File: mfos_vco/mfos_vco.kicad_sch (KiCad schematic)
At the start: 26 parts, among them Q1 SSM2210, U1 OP275

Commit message: Second Commit
nueva hoja
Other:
- added sheet P2 (untitled.kicad_sch)
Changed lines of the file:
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@@
+		)
+	)
+	(sheet
+		(at 5.08 276.86)
+		(size 289.56 184.15)
+		(fields_autoplaced yes)
+		(stroke
+			(width 0.1524)
+			(type solid)
+		)
+		(fill
+			(color 0 0 0 0.0000)
+		)
+		(property "Sheetname" "P2"
+			(at 5.08 276.1484 0)
+			(effects
+				(font
+					(size 1.27 1.27)
+				)
+				(justify left bottom)
+			)
+		)
+		(property "Sheetfile" "untitled.kicad_sch"
+			(at 5.08 461.5946 0)
+			(effects
+				(font
+					(size 1.27 1.27)
+				)
+				(justify left top)
+			)
+		)
+		(instances
+			(project "mfos_vco"
+				(path "/db27d43e-bcf4-48a8-8785-18123cee165a"
+					(page "2")
+				)
+			)
 		)
 	)

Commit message: update
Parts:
- added C1: 100p, symbol Device:C_Polarized_US
- added R1: 10K, symbol Device:R_US
- added U2: TL072, symbol Amplifier_Operational:TL072
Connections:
- net +12V: now also U2.8 (V+)
- net -12V: now also U2.4 (V-)
- net GND: now also U2.3 (+)
- net at Q1.1 (C1): now also C1.1, U2.2 (-)
- new net: R1.1, U2.5 (+)
- new net: C1.2, R1.2, U2.1

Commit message: added gitignore and updated to kicad 9
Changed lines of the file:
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@@
 (kicad_sch
-	(version 20231120)
+	(version 20250114)
 	(generator "eeschema")
-	(generator_version "8.0")
+	(generator_version "9.0")
 	(paper "A4")
+	(text "COARSE\n"
+		(exclude_from_sim no)
+		(at 64.516 63.246 0)
+		(effects
+			(font
+				(size 1.27 1.27)
+			)
+		)
+	)
+	(text "FINE\n"
+		(exclude_from_sim no)
+		(at 74.676 50.546 0)
+		(effects
+			(font
+				(size 1.27 1.27)
+			)
+		)
+	)
 	(junction
 		(at 86.36 123.19)
@@
 		)
 	)
-	(text "COARSE\n"
-		(exclude_from_sim no)
-		(at 64.516 63.246 0)
-		(effects
-			(font
-				(size 1.27 1.27)
-			)
-		)
-	)
-	(text "FINE\n"
-		(exclude_from_sim no)
-		(at 74.676 50.546 0)
-		(effects
-			(font
-				(size 1.27 1.27)
-			)
-		)
-	)
 	(global_label "CV3"
 		(shape input)
@@
 		(at 5.08 276.86)
 		(size 289.56 184.15)
+		(exclude_from_sim no)
+		(in_bom yes)
+		(on_board yes)
+		(dnp no)
 		(fields_autoplaced yes)
 		(stroke
@@
 		)
 	)
+	(embedded_fonts no)
 )

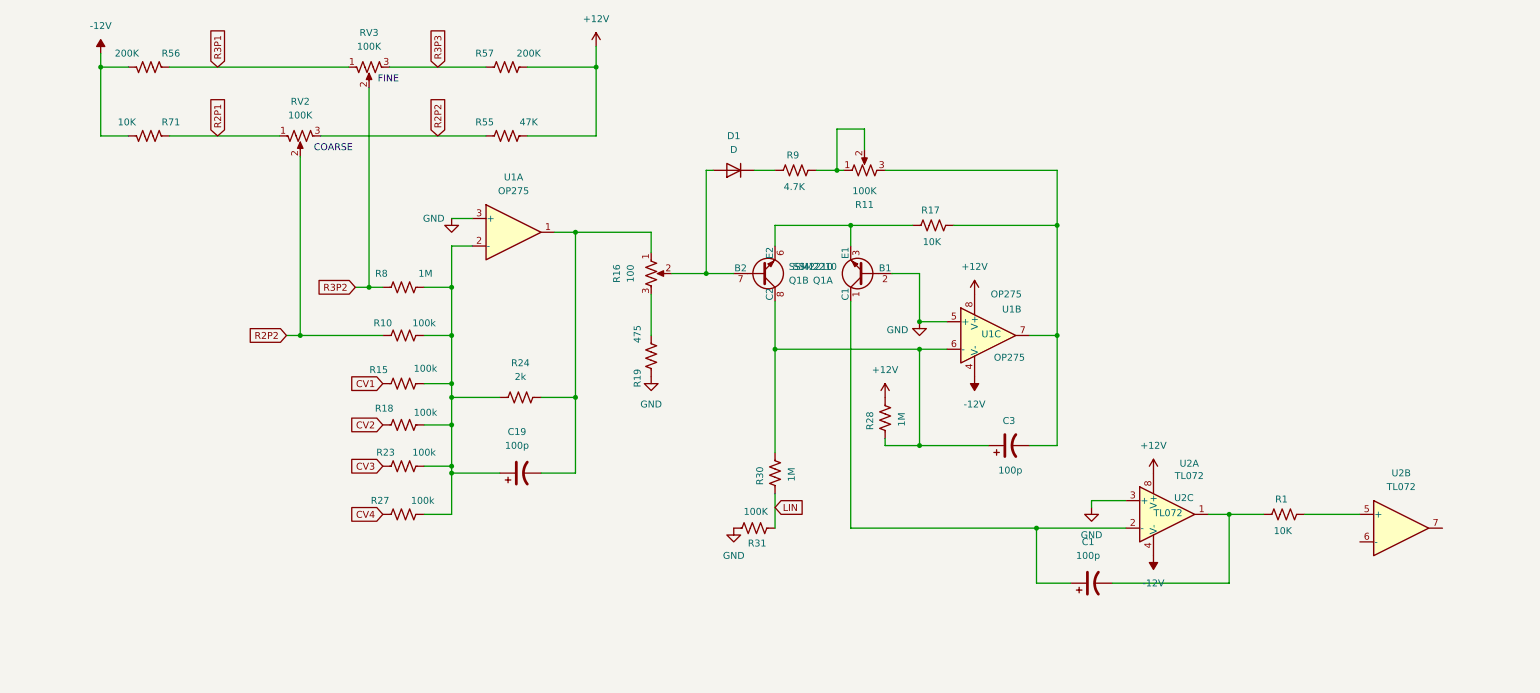
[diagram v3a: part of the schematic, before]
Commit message: finished first page. Added hierarchical sheets for first and second page
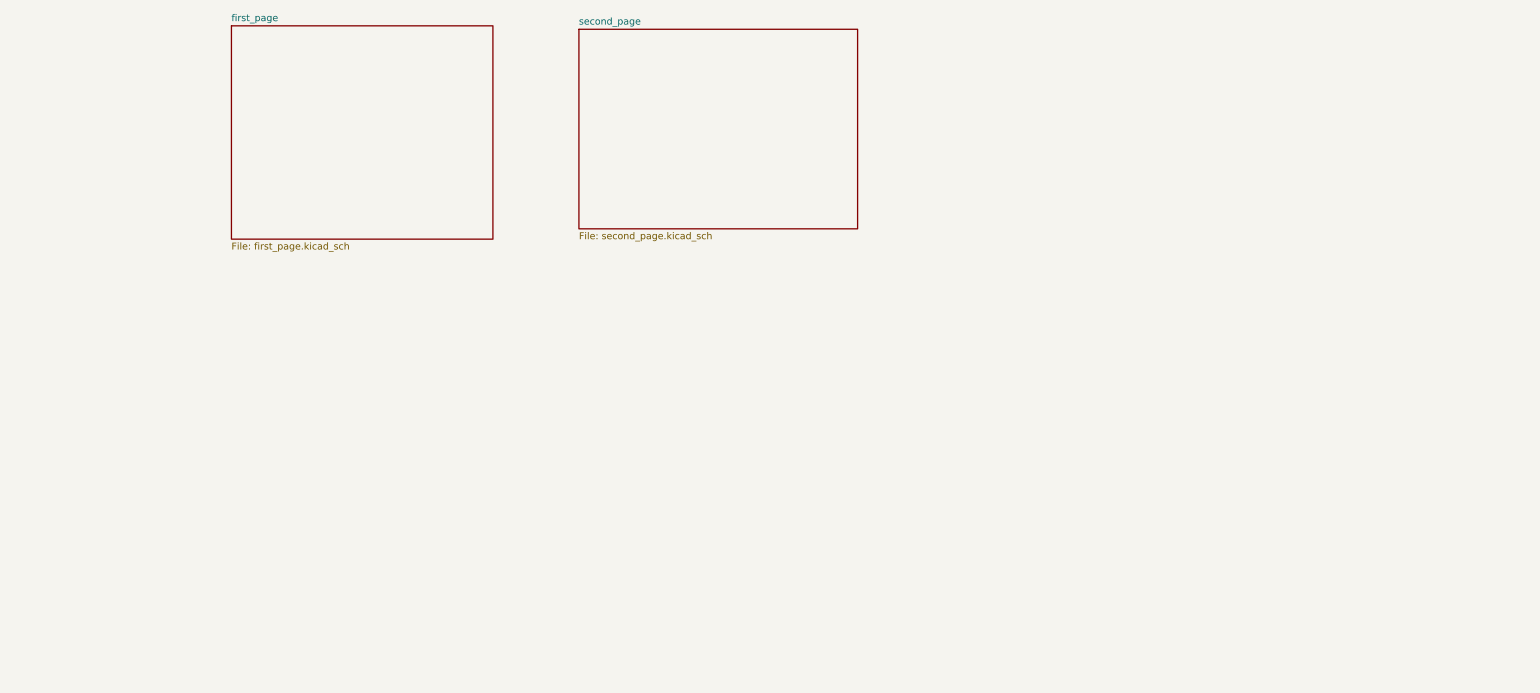
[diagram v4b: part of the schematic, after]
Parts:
- removed C1, C19, C3: 100p, symbol Device:C_Polarized_US
- removed D1: D, symbol Device:D
- removed Q1: SSM2210, symbol Transistor_BJT:SSM2210
- removed R1, R17, R71: 10K, symbol Device:R_US
- removed R10, R15, R18, R23, R27: 100k, symbol Device:R_US
- removed R11, RV2, RV3: 100K, symbol Device:R_Potentiometer_US
- removed R16: 100, symbol Device:R_Potentiometer_US
- removed R19: 475, symbol Device:R_US
- removed R24: 2k, symbol Device:R_US
- removed R28, R30, R8: 1M, symbol Device:R_US
- removed R31: 100K, symbol Device:R_US
- removed R55: 47K, symbol Device:R_US
- removed R56, R57: 200K, symbol Device:R_US
- removed R9: 4.7K, symbol Device:R_US
- removed U1: OP275, symbol Amplifier_Operational:OP275
- removed U2: TL072, symbol Amplifier_Operational:TL072
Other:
- added sheet first_page (first_page.kicad_sch)
- added sheet second_page (second_page.kicad_sch)
- note removed: "COARSE"
- note removed: "FINE"

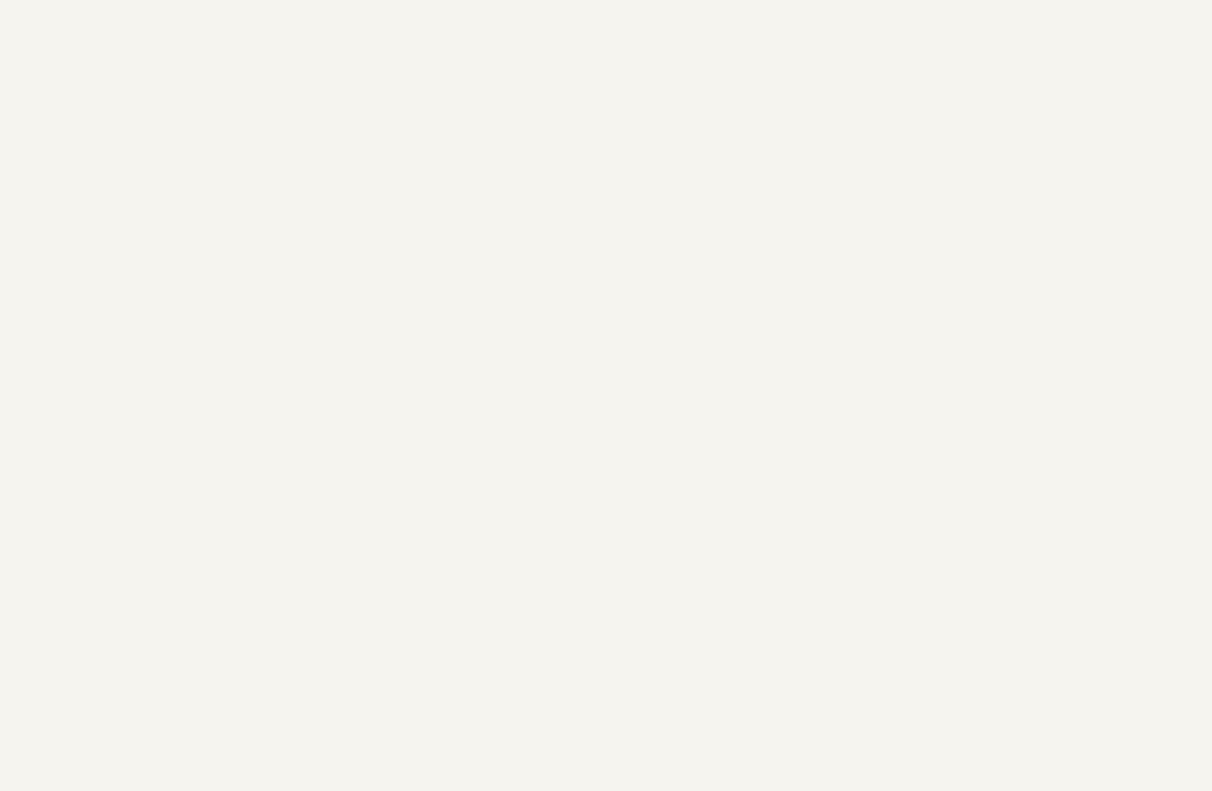
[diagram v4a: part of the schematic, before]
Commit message: Added output jumpers and custom foorprint
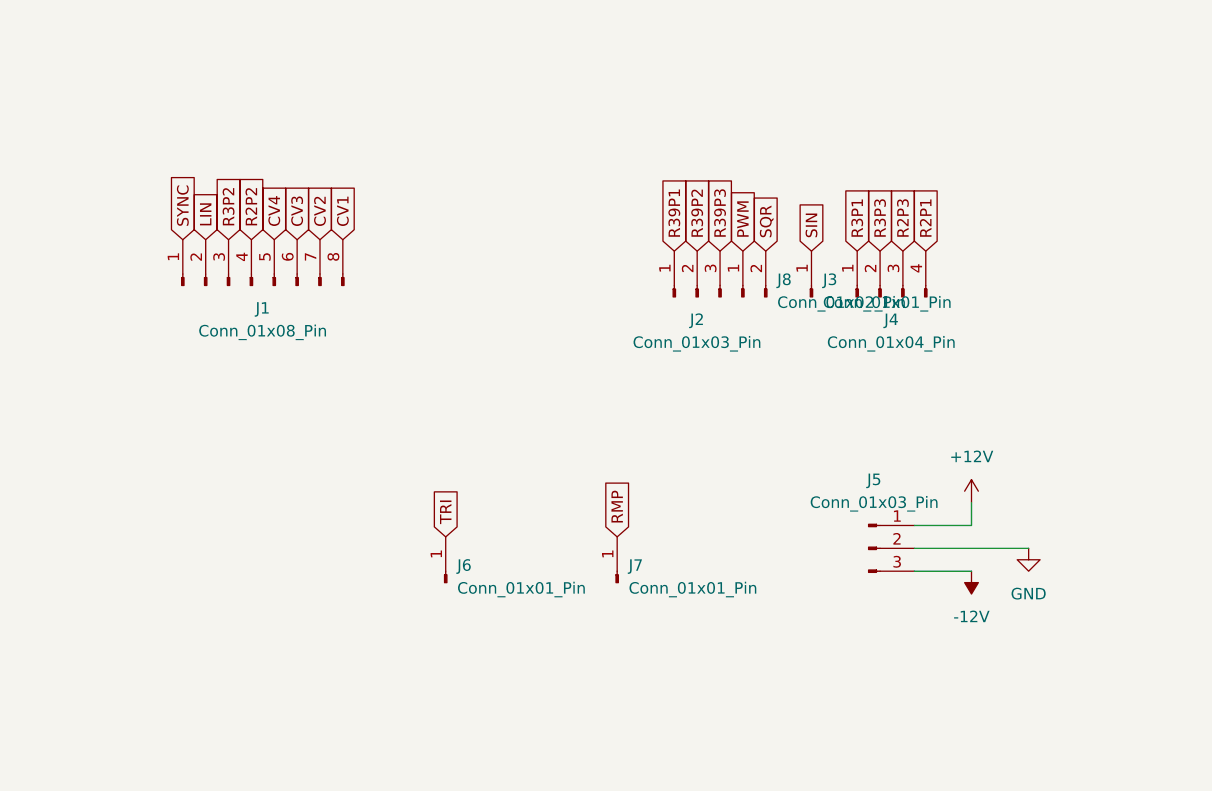
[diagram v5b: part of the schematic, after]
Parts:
- added J1: Conn_01x08_Pin, symbol Connector:Conn_01x08_Pin
- added J2, J5: Conn_01x03_Pin, symbol Connector:Conn_01x03_Pin
- added J3, J6, J7: Conn_01x01_Pin, symbol Connector:Conn_01x01_Pin
- added J4: Conn_01x04_Pin, symbol Connector:Conn_01x04_Pin
- added J8: Conn_01x02_Pin, symbol Connector:Conn_01x02_Pin
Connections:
- new net +12V: J5.1 (Pin_1)
- new net -12V: J5.3 (Pin_3)
- new net CV1: J1.8 (Pin_8)
- new net CV2: J1.7 (Pin_7)
- new net CV3: J1.6 (Pin_6)
- new net CV4: J1.5 (Pin_5)
- new net GND: J5.2 (Pin_2)
- new net LIN: J1.2 (Pin_2)
- new net PWM: J8.1 (Pin_1)
- new net R2P1: J4.4 (Pin_4)
- new net R2P2: J1.4 (Pin_4)
- new net R2P3: J4.3 (Pin_3)
- new net R39P1: J2.1 (Pin_1)
- new net R39P2: J2.2 (Pin_2)
- new net R39P3: J2.3 (Pin_3)
- new net R3P1: J4.1 (Pin_1)
- new net R3P2: J1.3 (Pin_3)
- new net R3P3: J4.2 (Pin_2)
- new net RMP: J7.1 (Pin_1)
- new net SIN: J3.1 (Pin_1)
- new net SQR: J8.2 (Pin_2)
- new net SYNC: J1.1 (Pin_1)
- new net TRI: J6.1 (Pin_1)

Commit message: added footprints
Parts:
- J1: footprint (none) -> Connector_PinSocket_2.54mm:PinSocket_1x08_P2.54mm_Vertical
- J2, J5: footprint (none) -> Connector_PinSocket_2.54mm:PinSocket_1x03_P2.54mm_Vertical
- J3, J6, J7: footprint (none) -> Connector_PinSocket_2.54mm:PinSocket_1x01_P2.54mm_Vertical
- J4: footprint (none) -> Connector_PinSocket_2.54mm:PinSocket_1x04_P2.54mm_Vertical
- J8: footprint (none) -> Connector_PinSocket_2.54mm:PinSocket_1x02_P2.54mm_Vertical
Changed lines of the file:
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@@
 			)
 		)
-		(property "Footprint" ""
+		(property "Footprint" "Connector_PinSocket_2.54mm:PinSocket_1x08_P2.54mm_Vertical"
 			(at 59.69 120.65 0)
 			(effects
@@
 			)
 		)
-		(property "Footprint" ""
+		(property "Footprint" "Connector_PinSocket_2.54mm:PinSocket_1x04_P2.54mm_Vertical"
 			(at 129.54 121.92 0)
 			(effects
@@
 			)
 		)
-		(property "Footprint" ""
+		(property "Footprint" "Connector_PinSocket_2.54mm:PinSocket_1x03_P2.54mm_Vertical"
 			(at 128.27 149.86 0)
 			(effects
@@
 			)
 		)
-		(property "Footprint" ""
+		(property "Footprint" "Connector_PinSocket_2.54mm:PinSocket_1x03_P2.54mm_Vertical"
 			(at 109.22 121.92 0)
 			(effects
@@
 			)
 		)
-		(property "Footprint" ""
+		(property "Footprint" "Connector_PinSocket_2.54mm:PinSocket_1x02_P2.54mm_Vertical"
 			(at 114.3 121.92 0)
 			(effects
@@
 			)
 		)
-		(property "Footprint" ""
+		(property "Footprint" "Connector_PinSocket_2.54mm:PinSocket_1x01_P2.54mm_Vertical"
 			(at 121.92 121.92 0)
 			(effects
@@
 			)
 		)
-		(property "Footprint" ""
+		(property "Footprint" "Connector_PinSocket_2.54mm:PinSocket_1x01_P2.54mm_Vertical"
 			(at 81.28 153.67 0)
 			(effects
@@
 			)
 		)
-		(property "Footprint" ""
+		(property "Footprint" "Connector_PinSocket_2.54mm:PinSocket_1x01_P2.54mm_Vertical"
 			(at 100.33 153.67 0)
 			(effects
